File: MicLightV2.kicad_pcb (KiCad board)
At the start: 4 copper layers, 84 x 103 mm, 130 parts, among them J1 12402012E212A, Q1 CSD87503Q3E, SW1 TL3365AF180QG, U1 UA78M33CKVURG3, U10 NCR321UX, U11 NCR321UX, U12 TC7PZ17FU, U2 AP33772DKZ-13, U3 STM32F072CBU6, U4 NCR321UX, U5 NCR321UX, U6 NCR321UX, U7 NCR321UX, U8 NCR321UX, U9 NCR321UX, Y1 16MHz

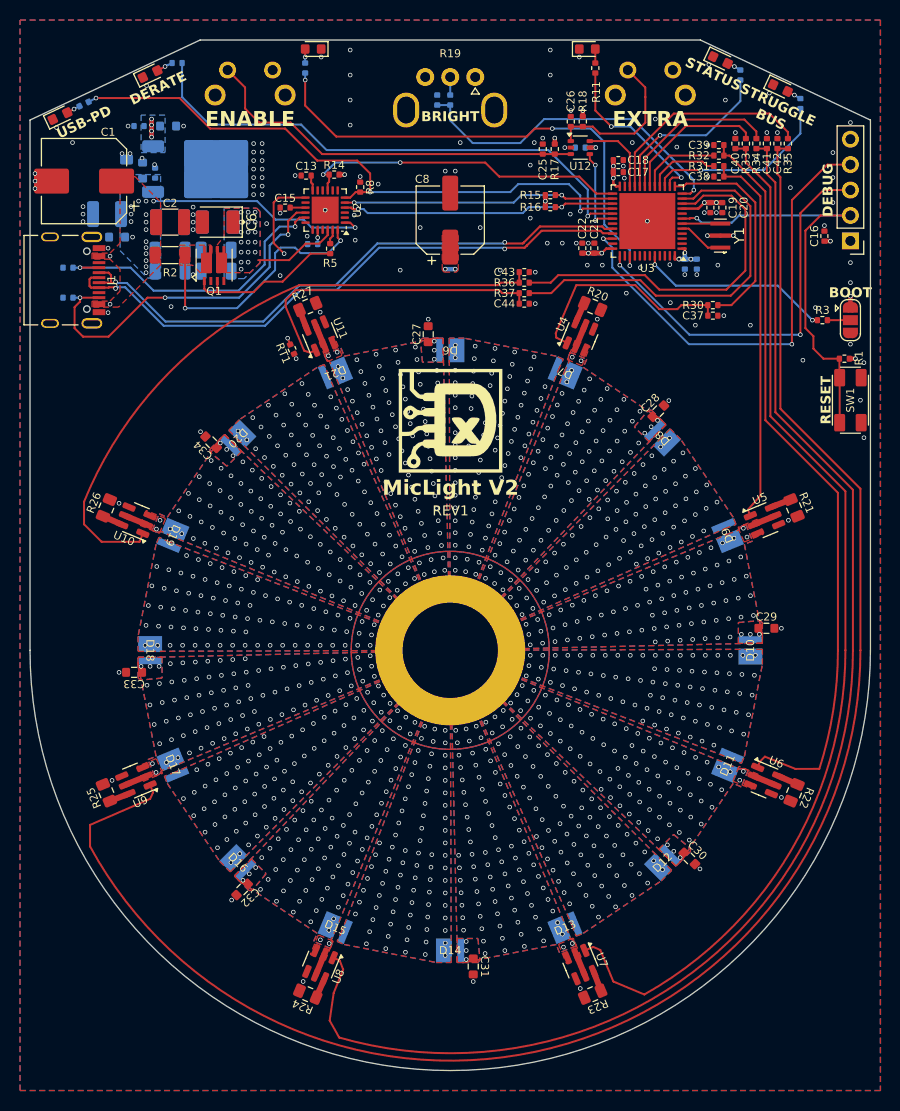
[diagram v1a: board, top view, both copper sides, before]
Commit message: REV2 - add DAC and cc led drivers
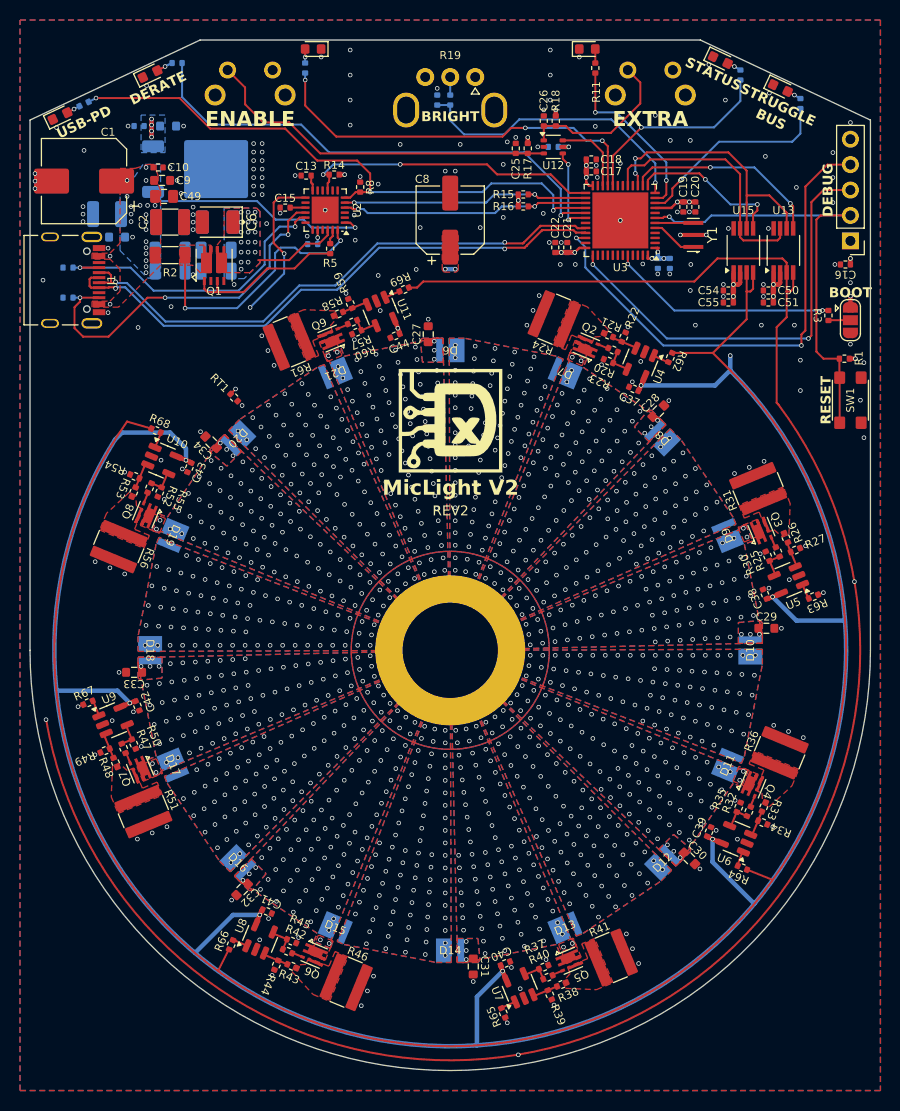
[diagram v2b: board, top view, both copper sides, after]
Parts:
- added C50: 100n, Daxxn_Standard_Capacitors:CAP_0402, F.Cu at (91.8, 44.0)
- added C51: 100n, Daxxn_Standard_Capacitors:CAP_0402, F.Cu at (91.8, 45.2)
- added C54: 100n, Daxxn_Standard_Capacitors:CAP_0402, F.Cu at (87.8, 44.0)
- added C55: 100n, Daxxn_Standard_Capacitors:CAP_0402, F.Cu at (87.8, 45.2)
- added Q2: SIA440DJ-T1-GE3, Daxxn_Packages:PowerPak_SC-70-6, F.Cu at (73.6, 49.6)
- added Q3: SIA440DJ-T1-GE3, Daxxn_Packages:PowerPak_SC-70-6, F.Cu at (91.1, 68.0)
- added Q4: SIA440DJ-T1-GE3, Daxxn_Packages:PowerPak_SC-70-6, F.Cu at (90.2, 93.4)
- added Q5: SIA440DJ-T1-GE3, Daxxn_Packages:PowerPak_SC-70-6, F.Cu at (71.9, 111.0)
- added Q6: SIA440DJ-T1-GE3, Daxxn_Packages:PowerPak_SC-70-6, F.Cu at (46.4, 110.4)
- added Q7: SIA440DJ-T1-GE3, Daxxn_Packages:PowerPak_SC-70-6, F.Cu at (29.0, 91.9)
- added Q8: SIA440DJ-T1-GE3, Daxxn_Packages:PowerPak_SC-70-6, F.Cu at (29.6, 66.4)
- added Q9: SIA440DJ-T1-GE3, Daxxn_Packages:PowerPak_SC-70-6, F.Cu at (48.1, 48.8)
- added R38: 1K 0.1%, Daxxn_Standard_Resistors:RES_0402, F.Cu at (71.1, 113.4)
- added R39: 10K 0.1%, Daxxn_Standard_Resistors:RES_0402, F.Cu at (70.0, 114.4)
- added R40: 10K, Daxxn_Standard_Resistors:RES_0402, F.Cu at (69.3, 111.6)
- added R41: 10, Daxxn_Standard_Resistors:RES_1218, F.Cu at (76.1, 110.7)
- added R42: 100, Daxxn_Standard_Resistors:RES_0402, F.Cu at (43.7, 110.1)
- added R43: 1K 0.1%, Daxxn_Standard_Resistors:RES_0402, F.Cu at (44.2, 111.5)
- added R44: 10K 0.1%, Daxxn_Standard_Resistors:RES_0402, F.Cu at (42.6, 111.4)
- added R45: 10K, Daxxn_Standard_Resistors:RES_0402, F.Cu at (44.2, 109.0)
- added R46: 10, Daxxn_Standard_Resistors:RES_1218, F.Cu at (49.6, 113.1)
- added R47: 100, Daxxn_Standard_Resistors:RES_0402, F.Cu at (27.4, 89.8)
- added R48: 1K 0.1%, Daxxn_Standard_Resistors:RES_0402, F.Cu at (26.5, 91.2)
- added R49: 10K 0.1%, Daxxn_Standard_Resistors:RES_0402, F.Cu at (25.5, 90.0)
- added R50: 10K, Daxxn_Standard_Resistors:RES_0402, F.Cu at (28.4, 89.3)
- added R51: 10, Daxxn_Standard_Resistors:RES_1218, F.Cu at (29.3, 96.1)
- added R52: 100, Daxxn_Standard_Resistors:RES_0402, F.Cu at (29.9, 63.7)
- added R53: 1K 0.1%, Daxxn_Standard_Resistors:RES_0402, F.Cu at (28.4, 64.2)
- added R54: 10K 0.1%, Daxxn_Standard_Resistors:RES_0402, F.Cu at (28.5, 62.6)
- added R55: 10K, Daxxn_Standard_Resistors:RES_0402, F.Cu at (31.0, 64.2)
- added R56: 10, Daxxn_Standard_Resistors:RES_1218, F.Cu at (26.9, 69.6)
- added R57: 100, Daxxn_Standard_Resistors:RES_0402, F.Cu at (50.2, 47.2)
- added R58: 1K 0.1%, Daxxn_Standard_Resistors:RES_0402, F.Cu at (48.8, 46.3)
- added R59: 10K 0.1%, Daxxn_Standard_Resistors:RES_0402, F.Cu at (50.0, 45.3)
- added R60: 10K, Daxxn_Standard_Resistors:RES_0402, F.Cu at (50.7, 48.2)
- added R61: 10, Daxxn_Standard_Resistors:RES_1218, F.Cu at (43.9, 49.1)
- added R62: 100, Daxxn_Standard_Resistors:RES_0402, F.Cu at (82.0, 50.7)
- added R63: 100, Daxxn_Standard_Resistors:RES_0402, F.Cu at (96.3, 74.6)
- added R64: 100, Daxxn_Standard_Resistors:RES_0402, F.Cu at (89.2, 101.7)
- added R65: 100, Daxxn_Standard_Resistors:RES_0402, F.Cu at (65.3, 116.2)
- added R66: 100, Daxxn_Standard_Resistors:RES_0402, F.Cu at (38.1, 109.4)
- added R67: 100, Daxxn_Standard_Resistors:RES_0402, F.Cu at (23.8, 85.2)
- added R68: 100, Daxxn_Standard_Resistors:RES_0402, F.Cu at (30.6, 58.0)
- added R69: 100, Daxxn_Standard_Resistors:RES_0402, F.Cu at (55.4, 43.9)
- added U13: DAC8551IADGKR, Daxxn_Packages:VSSOP-8_3.0x3.0mm_P0.65mm, F.Cu at (93.3, 40.0)
- added U15: DAC8551IADGKR, Daxxn_Packages:VSSOP-8_3.0x3.0mm_P0.65mm, F.Cu at (89.3, 40.0)
- C10, C49, C9: moved to F.Cu
- C37, C38, C39, C40, C41, C42, C43, C44: value 1u -> 100n
- R19: footprint Daxxn_Switches:PTV09A-2030F-A103 -> Daxxn_Controls_Pots:PTV09A-2030F-A103
- R20, R25: value 3 -> 100; footprint Daxxn_Standard_Resistors:RES_0805 -> Daxxn_Standard_Resistors:RES_0402
- R21, R26: value 3 -> 1K 0.1%; footprint Daxxn_Standard_Resistors:RES_0805 -> Daxxn_Standard_Resistors:RES_0402
- R22, R27: value 3 -> 10K 0.1%; footprint Daxxn_Standard_Resistors:RES_0805 -> Daxxn_Standard_Resistors:RES_0402
- R23: value 3 -> 10K; footprint Daxxn_Standard_Resistors:RES_0805 -> Daxxn_Standard_Resistors:RES_0402
- R24: value 3 -> 10; footprint Daxxn_Standard_Resistors:RES_0805 -> Daxxn_Standard_Resistors:RES_1218
- R31, R36: value 10K -> 10; footprint Daxxn_Standard_Resistors:RES_0402 -> Daxxn_Standard_Resistors:RES_1218
- R32, R37: value 10K -> 100
- R33: value 10K -> 1K 0.1%
- R34: value 10K -> 10K 0.1%
- S1, S2: footprint Daxxn_Switches:TL1105VF -> Daxxn_Controls_Buttons:TL1105VF
- SW1: footprint Daxxn_Switches:TL3365AF180QG -> Daxxn_Controls_Buttons:TL3365AF180QG
- U10, U11, U4, U5, U6, U7, U8, U9: value NCR321UX -> APX321WG-7; footprint Daxxn_Packages:TSOT-23-6 -> Daxxn_Packages:SOT-23-5
- moved C41 91.6 mm to (41.7, 106.1), turned to 157.5 degrees
- moved C42 85.1 mm to (28.7, 85.5), turned to 112.5 degrees
- moved C40 85.1 mm to (65.5, 111.3), turned to -157.5 degrees
- moved R24 71.8 mm to (70.4, 46.9)
- moved R25 71.3 mm to (92.7, 70.1)
- moved C39 68.6 mm to (85.9, 98.1), turned to -112.5 degrees
- moved R37 68.4 mm to (69.8, 112.6), turned to 22.5 degrees
- moved R26 68.0 mm to (93.6, 68.7), turned to 112.5 degrees
- moved R34 67.9 mm to (91.2, 97.2), turned to -22.5 degrees
- moved R35 66.5 mm to (88.8, 95.6), turned to 67.5 degrees
- moved R33 66.3 mm to (91.3, 95.6), turned to 67.5 degrees
- moved R32 65.6 mm to (89.9, 96.1), turned to 67.5 degrees
- moved R23 63.3 mm to (75.8, 51.1), turned to 157.5 degrees
- moved R27 54.5 mm to (94.5, 69.9)
- moved R36 53.5 mm to (92.9, 90.2), turned to 67.5 degrees
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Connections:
- C37 pad 1: Net-(U4-EN) -> GND
- C37 pad 2: GND -> VDD
- C38 pad 1: Net-(U5-EN) -> GND
- C38 pad 2: GND -> VDD
- C39 pad 1: Net-(U6-EN) -> GND
- C39 pad 2: GND -> VDD
- C40 pad 1: Net-(U7-EN) -> GND
- C40 pad 2: GND -> VDD
- C41 pad 1: Net-(U8-EN) -> GND
- C41 pad 2: GND -> VDD
- C42 pad 1: Net-(U9-EN) -> GND
- C42 pad 2: GND -> VDD
- C43 pad 1: Net-(U10-EN) -> GND
- C43 pad 2: GND -> VDD
- C44 pad 1: Net-(U11-EN) -> GND
- C44 pad 2: GND -> VDD
- R20 pad 1: Net-(U4-REXT) -> Net-(U4-OUT)
- R20 pad 2: GND -> Net-(Q2-G)
- R21 pad 1: Net-(U5-REXT) -> Net-(U4-IN-)
- R21 pad 2: GND -> Net-(Q2-S)
- R22 pad 1: Net-(U6-REXT) -> Net-(U4-IN-)
- R23 pad 1: Net-(U7-REXT) -> Net-(U4-OUT)
- R24 pad 1: Net-(U8-REXT) -> Net-(Q2-S)
- R25 pad 1: Net-(U9-REXT) -> Net-(U5-OUT)
- R25 pad 2: GND -> Net-(Q3-G)
- R26 pad 1: Net-(U10-REXT) -> Net-(U5-IN-)
- R26 pad 2: GND -> Net-(Q3-S)
- R27 pad 1: Net-(U11-REXT) -> Net-(U5-IN-)
- R30 pad 1: /LED1 -> Net-(U5-OUT)
- R30 pad 2: Net-(U4-EN) -> GND
- R31 pad 1: /LED2 -> Net-(Q3-S)
- R31 pad 2: Net-(U5-EN) -> GND
- R32 pad 1: /LED3 -> Net-(U6-OUT)
- R32 pad 2: Net-(U6-EN) -> Net-(Q4-G)
- R33 pad 1: /LED4 -> Net-(U6-IN-)
- R33 pad 2: Net-(U7-EN) -> Net-(Q4-S)
- R34 pad 1: /LED5 -> Net-(U6-IN-)
- R34 pad 2: Net-(U8-EN) -> GND
- R35 pad 1: /LED6 -> Net-(U6-OUT)
- R35 pad 2: Net-(U9-EN) -> GND
- R36 pad 1: /LED7 -> Net-(Q4-S)
- R36 pad 2: Net-(U10-EN) -> GND
- R37 pad 1: /LED8 -> Net-(U7-OUT)
- R37 pad 2: Net-(U11-EN) -> Net-(Q5-G)
- U10 pad 1: Net-(U10-EN) -> Net-(U10-IN+)
- U10 pad 2: Net-(D19-K) -> GND
- U10 pad 3: Net-(D19-K) -> Net-(U10-IN-)
- U10 pad 4: GND -> Net-(U10-OUT)
- U10 pad 5: Net-(D19-K) -> VDD
- U11 pad 1: Net-(U11-EN) -> Net-(U11-IN+)
- U11 pad 2: Net-(D21-K) -> GND
- U11 pad 3: Net-(D21-K) -> Net-(U11-IN-)
- U11 pad 4: GND -> Net-(U11-OUT)
- U11 pad 5: Net-(D21-K) -> VDD
- U3 pad 10: /LED7 -> /STRUGGLE-IND
- U3 pad 11: /LED8 -> /MAX-BRIGHT-IND
- U3 pad 13: /LED1 -> /DAC-HI-SYNC
- U3 pad 14: /MAX-BRIGHT-IND -> /DAC-LO-SYNC
- U3 pad 15: /STRUGGLE-IND -> /DAC-SCLK
- U3 pad 16: /LED2 -> unconnected-(U3B-PA6-Pad16)
- U3 pad 17: /LED3 -> /DAC-SDIN
- U3 pad 18: /LED4 -> unconnected-(U3B-PB0-Pad18)
- U3 pad 19: /LED5 -> unconnected-(U3B-PB1-Pad19)
- U3 pad 21: /LED6 -> /ENABLE-IND
- U3 pad 39: /ENABLE-IND -> unconnected-(U3B-PB3-Pad39)
- U4 pad 1: Net-(U4-EN) -> Net-(U4-IN+)
- U4 pad 2: Net-(D7-K) -> GND
- U4 pad 3: Net-(D7-K) -> Net-(U4-IN-)
- U4 pad 4: GND -> Net-(U4-OUT)
- U4 pad 5: Net-(D7-K) -> VDD
- U5 pad 1: Net-(U5-EN) -> Net-(U5-IN+)
- U5 pad 2: Net-(D9-K) -> GND
- U5 pad 3: Net-(D9-K) -> Net-(U5-IN-)
- U5 pad 4: GND -> Net-(U5-OUT)
- U5 pad 5: Net-(D9-K) -> VDD
- U6 pad 1: Net-(U6-EN) -> Net-(U6-IN+)
- U6 pad 2: Net-(D11-K) -> GND
- U6 pad 3: Net-(D11-K) -> Net-(U6-IN-)
- U6 pad 4: GND -> Net-(U6-OUT)
- U6 pad 5: Net-(D11-K) -> VDD
- U7 pad 1: Net-(U7-EN) -> Net-(U7-IN+)
- U7 pad 2: Net-(D13-K) -> GND
- U7 pad 3: Net-(D13-K) -> Net-(U7-IN-)
- U7 pad 4: GND -> Net-(U7-OUT)
- U7 pad 5: Net-(D13-K) -> VDD
- U8 pad 1: Net-(U8-EN) -> Net-(U8-IN+)
- U8 pad 2: Net-(D15-K) -> GND
- U8 pad 3: Net-(D15-K) -> Net-(U8-IN-)
- U8 pad 4: GND -> Net-(U8-OUT)
- U8 pad 5: Net-(D15-K) -> VDD
- U9 pad 1: Net-(U9-EN) -> Net-(U9-IN+)
- U9 pad 2: Net-(D17-K) -> GND
- U9 pad 3: Net-(D17-K) -> Net-(U9-IN-)
- U9 pad 4: GND -> Net-(U9-OUT)
- U9 pad 5: Net-(D17-K) -> VDD
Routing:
- net VDD: track 34.9 -> 126.8 mm, vias 21 -> 34
- net Net-(U9-EN): track 64.8 -> 0.00 mm
- net Net-(U7-EN): track 63.8 -> 0.00 mm
- net Net-(U8-EN): track 63.7 -> 0.00 mm
- net Net-(U6-EN): track 62.5 -> 0.00 mm
- net /LEDS/DAC-OUT-LO: track 0.00 -> 56.2 mm, vias 0 -> 6
- net /LED8: track 38.9 -> 0.00 mm
- net Net-(U5-EN): track 38.0 -> 0.00 mm
- net /LED7: track 36.6 -> 0.00 mm
- net Net-(U10-EN): track 32.6 -> 0.00 mm
- net Net-(U11-EN): track 31.6 -> 0.00 mm
- net /DAC-SCLK: track 0.00 -> 27.0 mm, vias 0 -> 2
- net /DAC-SDIN: track 0.00 -> 25.4 mm
- net Net-(U4-EN): track 22.2 -> 0.00 mm
- net /LED6: track 21.7 -> 0.00 mm
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- added copper zone on F.Cu, net Net-(Q2-S)
- added copper zone on F.Cu, net Net-(Q3-S)
- added copper zone on F.Cu, net Net-(Q4-S)
- added copper zone on F.Cu, net Net-(Q5-S)
- added copper zone on F.Cu, net Net-(Q6-S)
- added copper zone on F.Cu, net Net-(Q7-S)
- added copper zone on F.Cu, net Net-(Q8-S)
- added copper zone on F.Cu, net Net-(Q9-S)
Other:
- board text added: "REV${REVISION}"
- board text removed: "REV1"
